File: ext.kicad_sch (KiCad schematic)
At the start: 34 parts, among them J4 0826-1X1T-GH-F, U10 LTC6820HMS, U11 LTC6820HMS, U12 LTC6820HMS, U13 AP1117-33, U9 LTC6820HMS

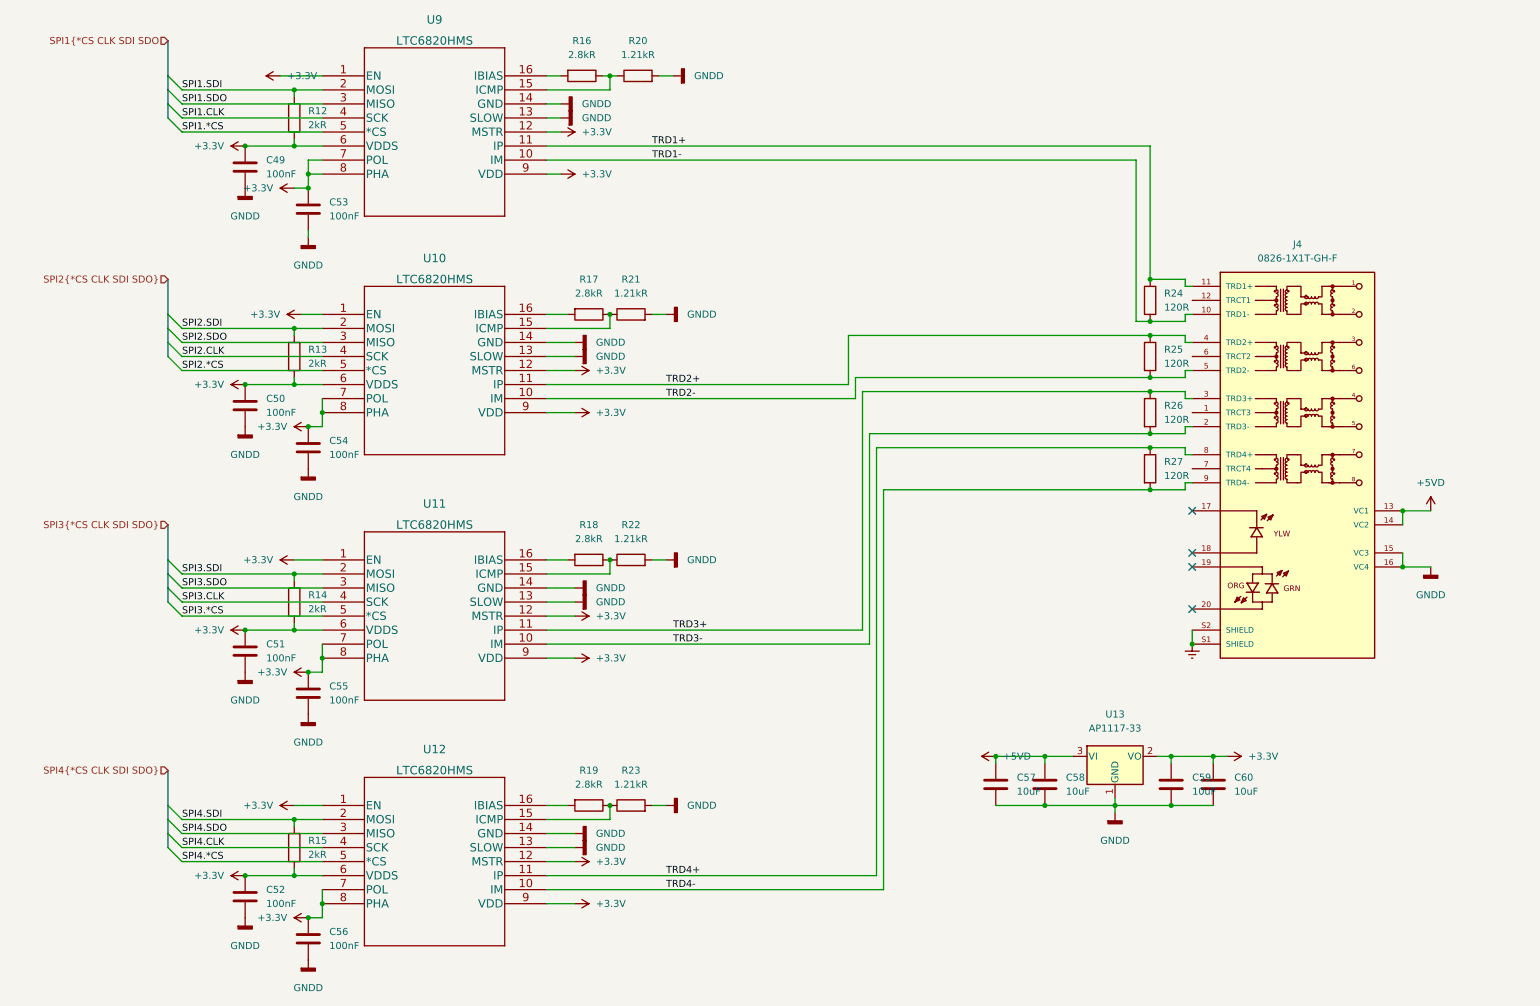
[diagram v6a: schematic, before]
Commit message: fix a few warnings
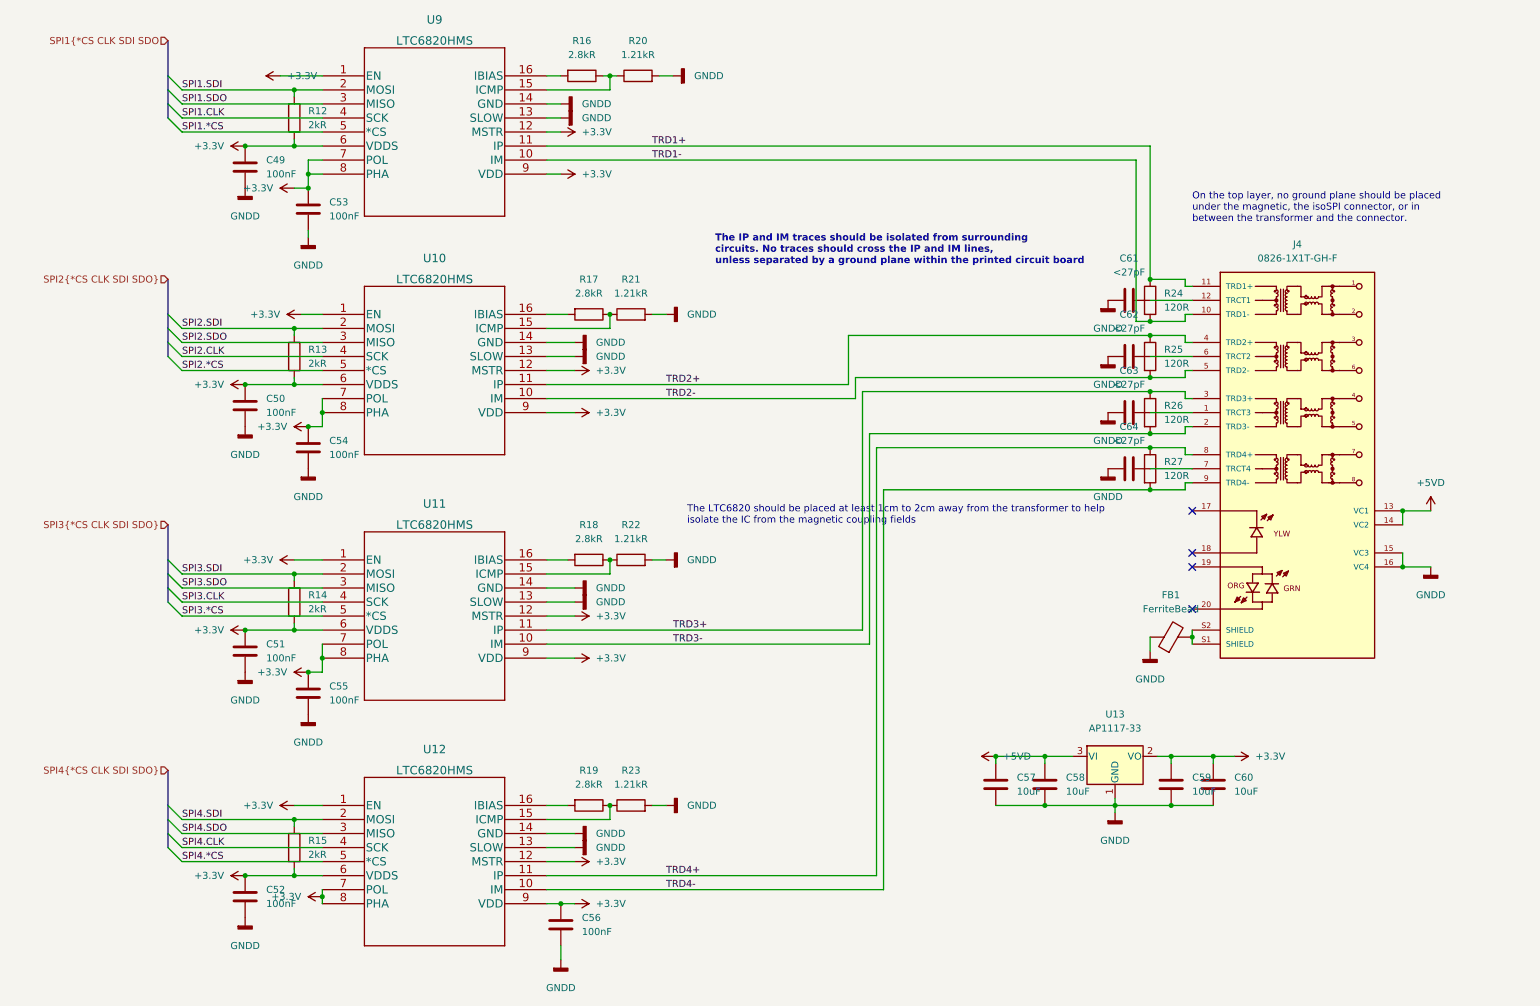
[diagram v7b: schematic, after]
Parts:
- added C61, C62, C63, C64: <27pF, Capacitor_SMD:C_0603_1608Metric, symbol Device:C
- added FB1: FerriteBead, Resistor_SMD:R_0805_2012Metric, symbol Device:FerriteBead
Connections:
- net GNDD: now also C61.1, C62.1, C63.1, C64.1, FB1.1
- net at J4.1 (TRCT3): now also C63.2
- net at J4.12 (TRCT1): now also C61.2
- net at J4.6 (TRCT2): now also C62.2
- net at J4.7 (TRCT4): now also C64.2
- net +3.3V renamed +3V3
- net Earth: no longer names the net of J4.S1 (SHIELD), J4.S2 (SHIELD)
- net Earth: now also FB1.2
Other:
- note added: "On the top layer, no ground plane should be placed under the magnetic, the isoSPI connector, or in between the transformer and the connector."
- note added: "The IP and IM traces should be isolated from surrounding circuits. No traces should cross the IP and IM lines, unless separated by a ground plane within the printed circuit board"
- note added: "The LTC6820 should be placed at least 1cm to 2cm away from the transformer to help isolate the IC from the magnetic coupling fields"
- moved on the sheet: C56

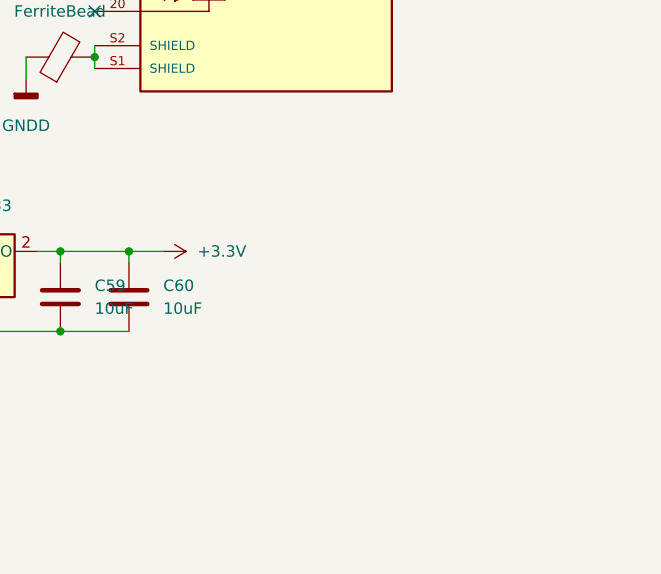
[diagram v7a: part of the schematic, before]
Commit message: add KK connectors for power (check voltage or bypass)
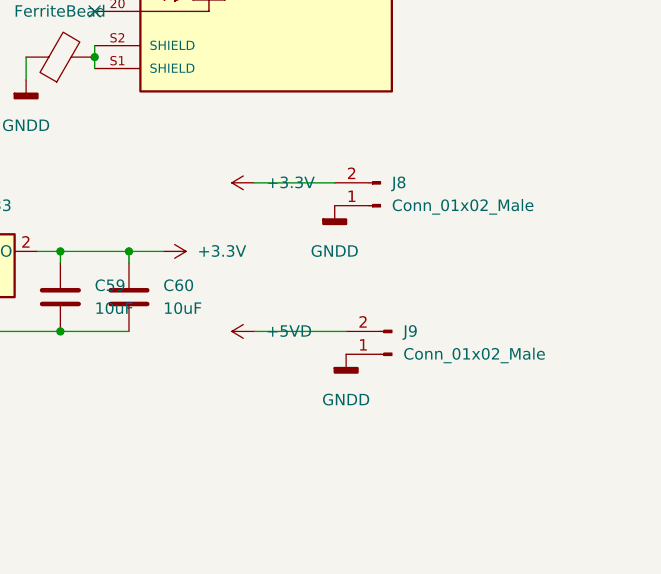
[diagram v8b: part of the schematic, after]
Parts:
- added J8, J9: Conn_01x02_Male, Connector_Molex:Molex_KK-254_AE-6410-02A_1x02_P2.54mm_Vertical, symbol Connector:Conn_01x02_Male
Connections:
- net +3V3: now also J8.2 (Pin_2)
- net +5VD: now also J9.2 (Pin_2)
- net GNDD: now also J8.1 (Pin_1), J9.1 (Pin_1)
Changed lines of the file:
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@@
+    (stroke (width 0) (type default) (color 0 0 0 0))
+  )
+  (wire (pts (xy 248.92 139.7) (xy 257.81 139.7))
     (stroke (width 0) (type default) (color 0 0 0 0))
   )
@@
   )
   (wire (pts (xy 114.3 24.13) (xy 116.84 24.13))
+    (stroke (width 0) (type default) (color 0 0 0 0))
+  )
+  (wire (pts (xy 248.92 156.21) (xy 259.08 156.21))
     (stroke (width 0) (type default) (color 0 0 0 0))
   )
@@
     )
     (property "Datasheet" "" (id 3) (at 73.66 172.72 0)
+      (effects (font (size 1.27 1.27)) hide)
+    )
+    (pin "1")
+  )
+  (symbol (lib_id "power:GNDD") (at 257.81 142.24 0) (unit 1)
+    (in_bom yes) (on_board yes) (fields_autoplaced)
+    (property "Reference" "#PWR072" (id 0) (at 257.81 148.59 0)
+      (effects (font (size 1.27 1.27)) hide)
+    )
+    (property "Value" "GNDD" (id 1) (at 257.81 147.32 0))
+    (property "Footprint" "" (id 2) (at 257.81 142.24 0)
+      (effects (font (size 1.27 1.27)) hide)
+    )
+    (property "Datasheet" "" (id 3) (at 257.81 142.24 0)
       (effects (font (size 1.27 1.27)) hide)
     )
@@
     (pin "1")
   )
+  (symbol (lib_id "Connector:Conn_01x02_Male") (at 262.89 142.24 180) (unit 1)
+    (in_bom yes) (on_board yes) (fields_autoplaced)
+    (property "Reference" "J8" (id 0) (at 264.16 139.6999 0)
+      (effects (font (size 1.27 1.27)) (justify right))
+    )
+    (property "Value" "Conn_01x02_Male" (id 1) (at 264.16 142.2399 0)
+      (effects (font (size 1.27 1.27)) (justify right))
+    )
+    (property "Footprint" "Connector_Molex:Molex_KK-254_AE-6410-02A_1x02_P2.54mm_Vertical" (id 2) (at 262.89 142.24 0)
+      (effects (font (size 1.27 1.27)) hide)
+    )
+    (property "Datasheet" "~" (id 3) (at 262.89 142.24 0)
+      (effects (font (size 1.27 1.27)) hide)
+    )
+    (pin "1")
+    (pin "2")
+  )
+  (symbol (lib_id "power:+5VD") (at 248.92 156.21 90) (unit 1)
+    (in_bom yes) (on_board yes) (fields_autoplaced)
+    (property "Reference" "#PWR069" (id 0) (at 252.73 156.21 0)
+      (effects (font (size 1.27 1.27)) hide)
+    )
+    (property "Value" "+5VD" (id 1) (at 250.19 156.2099 90)
+      (effects (font (size 1.27 1.27)) (justify right))
+    )
+    (property "Footprint" "" (id 2) (at 248.92 156.21 0)
+      (effects (font (size 1.27 1.27)) hide)
+    )
+    (property "Datasheet" "" (id 3) (at 248.92 156.21 0)
+      (effects (font (size 1.27 1.27)) hide)
+    )
+    (pin "1")
+  )
   (symbol (lib_id "power:+3.3V") (at 116.84 34.29 270) (unit 1)
     (in_bom yes) (on_board yes) (fields_autoplaced)
@@
     (pin "1")
   )
+  (symbol (lib_id "power:GNDD") (at 259.08 158.75 0) (unit 1)
+    (in_bom yes) (on_board yes) (fields_autoplaced)
+    (property "Reference" "#PWR073" (id 0) (at 259.08 165.1 0)
+      (effects (font (size 1.27 1.27)) hide)
+    )
+    (property "Value" "GNDD" (id 1) (at 259.08 163.83 0))
+    (property "Footprint" "" (id 2) (at 259.08 158.75 0)
+      (effects (font (size 1.27 1.27)) hide)
+    )
+    (property "Datasheet" "" (id 3) (at 259.08 158.75 0)
+      (effects (font (size 1.27 1.27)) hide)
+    )
+    (pin "1")
+  )
   (symbol (lib_id "Device:R") (at 120.65 24.13 270) (unit 1)
     (in_bom yes) (on_board yes) (fields_autoplaced)
@@
     (pin "1")
   )
+  (symbol (lib_id "power:+3.3V") (at 248.92 139.7 90) (unit 1)
+    (in_bom yes) (on_board yes) (fields_autoplaced)
+    (property "Reference" "#PWR067" (id 0) (at 252.73 139.7 0)
+      (effects (font (size 1.27 1.27)) hide)
+    )
+    (property "Value" "+3.3V" (id 1) (at 250.19 139.6999 90)
+      (effects (font (size 1.27 1.27)) (justify right))
+    )
+    (property "Footprint" "" (id 2) (at 248.92 139.7 0)
+      (effects (font (size 1.27 1.27)) hide)
+    )
+    (property "Datasheet" "" (id 3) (at 248.92 139.7 0)
+      (effects (font (size 1.27 1.27)) hide)
+    )
+    (pin "1")
+  )
   (symbol (lib_id "Device:R") (at 129.54 156.21 90) (unit 1)
     (in_bom yes) (on_board yes) (fields_autoplaced)
@@
       (effects (font (size 1.27 1.27)) hide)
     )
+    (pin "1")
+    (pin "2")
+  )
+  (symbol (lib_id "Connector:Conn_01x02_Male") (at 264.16 158.75 180) (unit 1)
+    (in_bom yes) (on_board yes) (fields_autoplaced)
+    (property "Reference" "J9" (id 0) (at 265.43 156.2099 0)
+      (effects (font (size 1.27 1.27)) (justify right))
+    )
+    (property "Value" "Conn_01x02_Male" (id 1) (at 265.43 158.7499 0)
+      (effects (font (size 1.27 1.27)) (justify right))
+    )
+    (property "Footprint" "Connector_Molex:Molex_KK-254_AE-6410-02A_1x02_P2.54mm_Vertical" (id 2) (at 264.16 158.75 0)
+      (effects (font (size 1.27 1.27)) hide)
+    )
+    (property "Datasheet" "~" (id 3) (at 264.16 158.75 0)
+      (effects (font (size 1.27 1.27)) hide)
+    )
